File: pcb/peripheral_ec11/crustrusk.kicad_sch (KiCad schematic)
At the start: 2 parts, among them P1 Conn_01x06_Socket

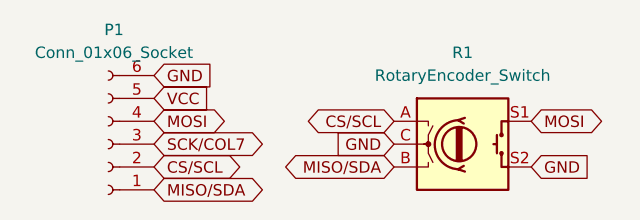
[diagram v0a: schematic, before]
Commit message: changed mainboard jst socket direction, added mousebite
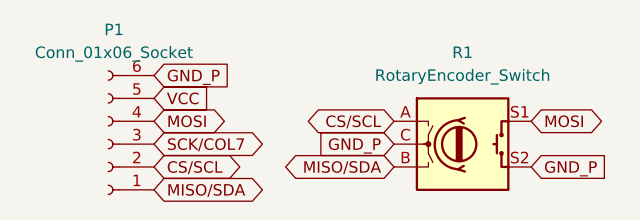
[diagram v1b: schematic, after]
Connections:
- net GND renamed GND_P
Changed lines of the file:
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@@
 		)
 	)
-	(global_label "GND"
+	(global_label "GND_P"
 		(shape input)
 		(at 55.88 29.21 180)
@@
 		)
 		(property "Intersheetrefs" "${INTERSHEET_REFS}"
-			(at 49.0243 29.21 0)
+			(at 46.7867 29.21 0)
 			(hide yes)
 			(show_name no)
@@
 		)
 	)
-	(global_label "GND"
+	(global_label "GND_P"
 		(shape input)
 		(at 71.12 31.75 0)
@@
 		)
 		(property "Intersheetrefs" "${INTERSHEET_REFS}"
-			(at 77.9757 31.75 0)
+			(at 80.2133 31.75 0)
 			(hide yes)
 			(show_name no)
@@
 		)
 	)
-	(global_label "GND"
+	(global_label "GND_P"
 		(shape input)
 		(at 29.21 21.59 0)
@@
 		)
 		(property "Intersheetrefs" "${INTERSHEET_REFS}"
-			(at 36.0657 21.59 0)
+			(at 38.3033 21.59 0)
 			(hide yes)
 			(show_name no)
